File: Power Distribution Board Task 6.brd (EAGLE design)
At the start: 71.8 x 64 mm, 25 parts, among them U2 MIC29300-5.0WU, U3 MIC29300-12WU, X1 5566-2, X2 5566-2, X4 C-GRID-02-15-19, X5 C-GRID-02-15-19, X6 C-GRID-02-15-19

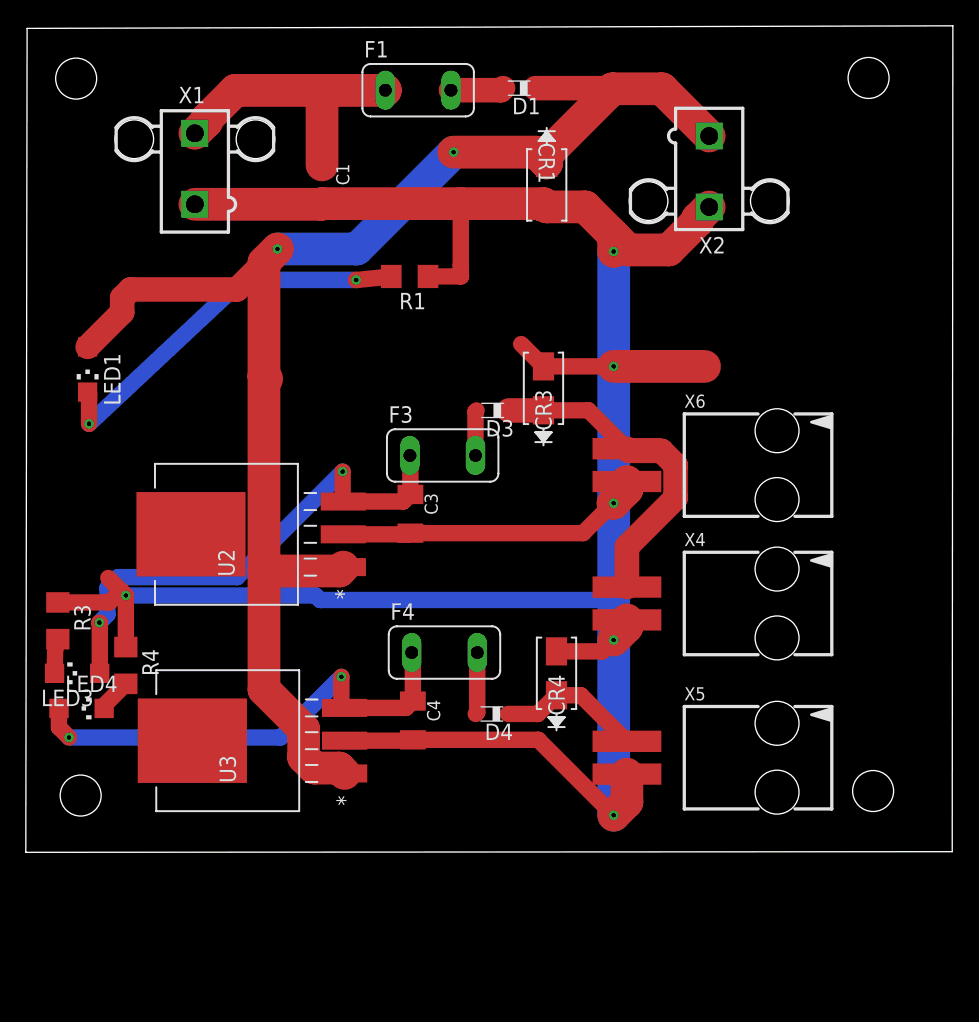
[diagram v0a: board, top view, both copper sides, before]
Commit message: removed 3.3V regulation, corrected name tags, switched 5V regulator, removed terminal connectors (DAN will make surface mount pad in the layout)
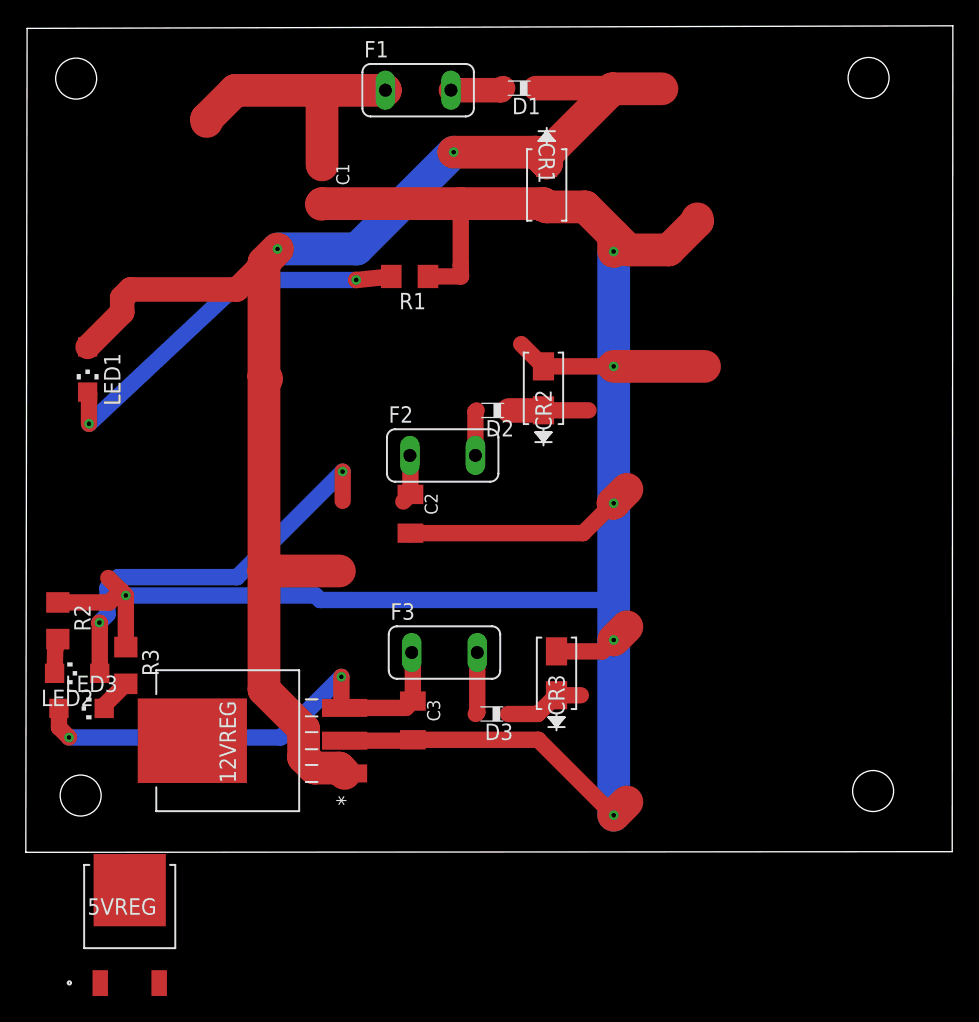
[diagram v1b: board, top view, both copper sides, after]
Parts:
- removed C4: 47uF, rcl:C1206K
- removed CR4: SMAJ5.0, SMAJ5_diode:SMASERIES
- removed D4: BAT60J, diode:SOD323_ST
- removed F4: (no value), fuse:TE5
- removed LED4: Yellow, led:CHIPLED_1206
- removed R4: 560, rcl:R1206
- removed U2: MIC29300-5.0WU, MIC29300_5v:TO-263-3
- removed X1, X2: 5566-2, con-molex:5566-2
- removed X4, X5, X6: C-GRID-02-15-19, con-molex:15-91-02
- added 5VREG: AP1084D18G-13, AP108412v_5v:TO252-3L
- added C2: 47uF, rcl:C1206K
- added CR2: SMAJ5.0, SMAJ5_diode:SMASERIES
- added D2: BAT60J, diode:SOD323_ST
- added F2: 6.25A, fuse:TE5
- added LED2: Red, led:CHIPLED_1206
- added R2: 150, rcl:R1206
- F1: value (none) -> 25A
- F3: value (none) -> 3A
- LED3: value Red -> Yellow
- R3: value 150 -> 560
- moved D3 23.5 mm to (35.1, 15.6)
- moved CR3 22.1 mm to (40.1, 18.7)
- moved C3 16.0 mm to (28.9, 15.1)
- moved F3 15.3 mm to (31.4, 20.3)
- moved R3 6.30 mm to (6.70, 19.3)
- moved LED3 2.74 mm to (3.27, 16.0), turned to 270 degrees
- renumbered U3 to 12VREG
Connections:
- removed net N$17 (its old number): D4.A, F4.2
- removed net N$20 (its old number): LED4.C, R4.2
- removed net V+: 12VREG.1, CR1.1, D1.C, LED1.A, U2.1, X2.1
- new net 12V+: 12VREG.1, 5VREG.3, CR1.1, D1.C, LED1.A
- new net N$12: D2.A, F2.2
- new net N$15: LED2.C, R2.2
- net GND: now also 5VREG.1, C2.2, CR2.2, R2.1; no longer C4.2, CR4.2, R4.1, U2.2, X1.1, X2.2, X4.2, X5.2, X6.2
- net N$13: now also CR2.1, D2.C; no longer CR3.1, D3.C, X4.1, X6.1
- net N$18: now also CR3.1, D3.C; no longer CR4.1, D4.C, X5.1
- net VOUT2: now also 5VREG.2, C2.1, F2.1, LED2.A; no longer C3.1, F3.1, LED3.A, U2.3
- net VOUT3: now also C3.1, F3.1, LED3.A; no longer C4.1, F4.1, LED4.A
- net VSTART: no longer X1.2
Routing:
- net V+: track 117.0 -> 0.00 mm, vias 2 -> 0
- net 12V+: track 0.00 -> 111.4 mm, vias 0 -> 2
- net N$13: track 25.7 -> 6.17 mm
- net GND: track 220.2 -> 200.7 mm
- net N$18: track 11.3 -> 6.25 mm
- net N$17 (its old number): track 4.81 -> 0.00 mm
- net VOUT2: track 39.7 -> 34.9 mm
- net N$12: track 0.00 -> 3.53 mm
- net N$15: track 0.00 -> 2.67 mm
- net N$20 (its old number): track 2.60 -> 0.00 mm
- net VSTART: track 22.1 -> 20.8 mm
- net N$17: track 3.53 -> 4.81 mm
